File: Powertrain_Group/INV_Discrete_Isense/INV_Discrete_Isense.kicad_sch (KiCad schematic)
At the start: 20 parts, among them J1 Conn_01x04_Socket, J2 Conn_01x04_Socket, J3 Conn_01x04_Socket, J4 15130122601000, J5 DF1E-2P-2.5DS_35_, J6 DF1E-2P-2.5DS_35_, U7 AMC3330

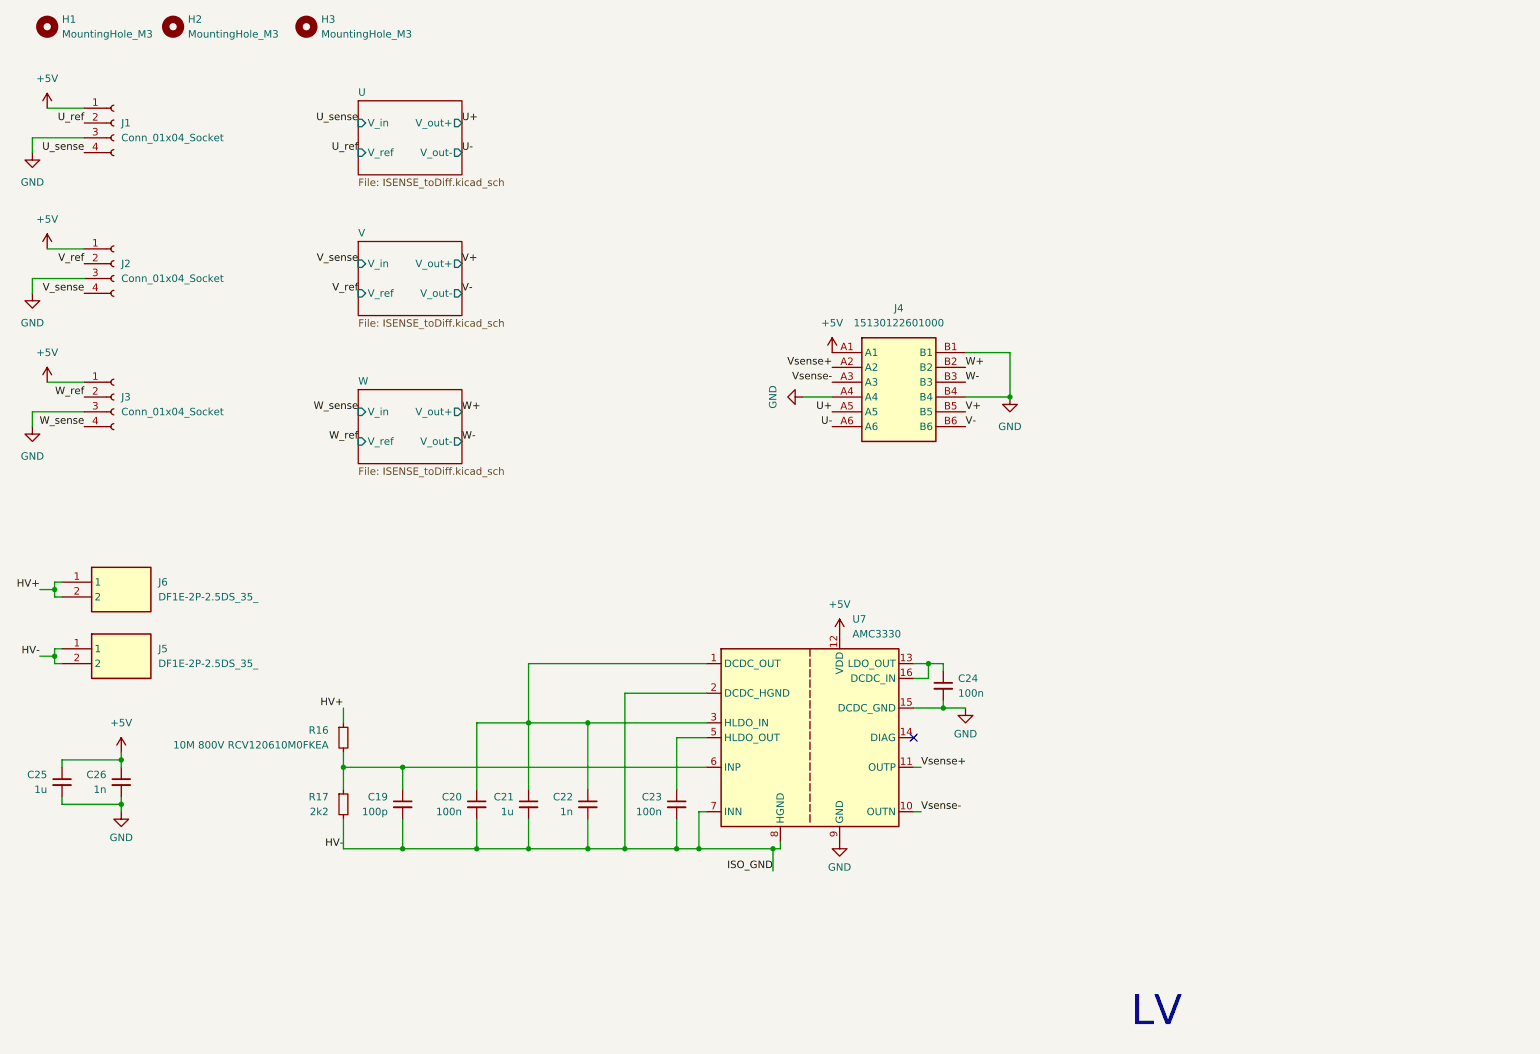
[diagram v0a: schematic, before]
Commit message: [INV_Discrete_Isense] V1.1
and update library for it
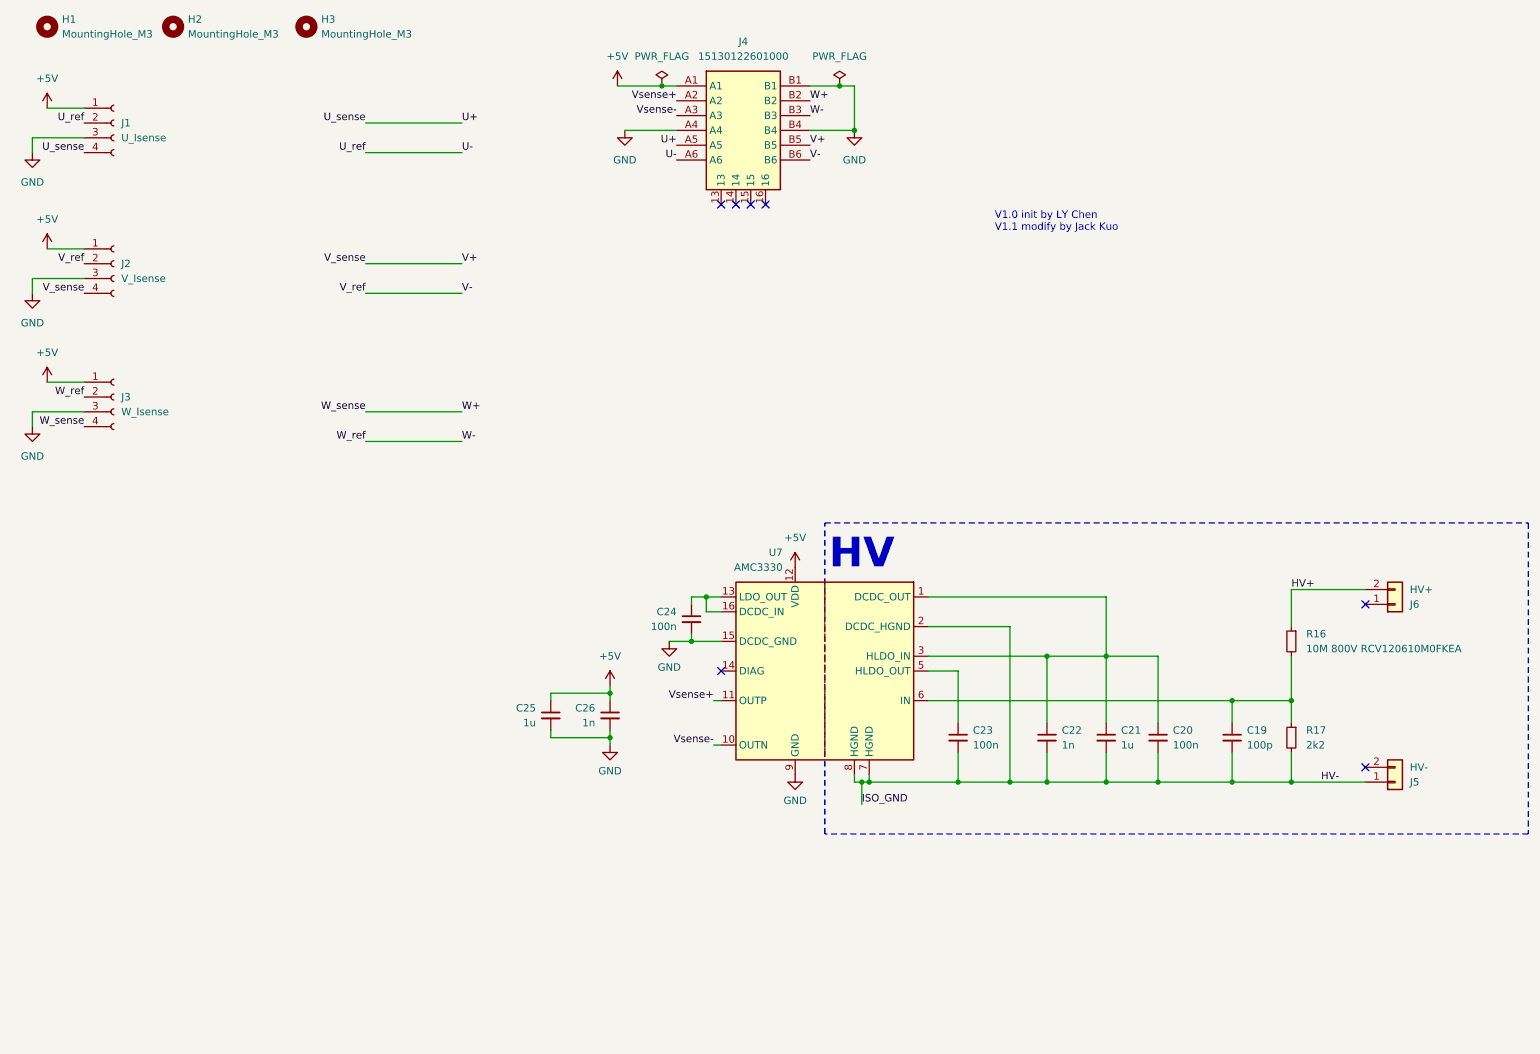
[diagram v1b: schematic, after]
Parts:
- J1: value Conn_01x04_Socket -> U_Isense
- J2: value Conn_01x04_Socket -> V_Isense
- J3: value Conn_01x04_Socket -> W_Isense
- J4: footprint 15130122601000 -> nturt_kicad_lib_EP7:Harting_15130122601000; symbol 15130122601000:15130122601000 -> nturt_kicad_lib_EP7:Harting_15130122601000
- J5: value DF1E-2P-2.5DS_35_ -> HV-; footprint DF1E2P25DS35 -> nturt_kicad_lib_EP7:Hirose_DF1E2P25DS35; symbol DF1E-2P-2_5DS_35_:DF1E-2P-2.5DS_35_ -> Connector_Generic:Conn_01x02
- J6: value DF1E-2P-2.5DS_35_ -> HV+; footprint DF1E2P25DS35 -> nturt_kicad_lib_EP7:Hirose_DF1E2P25DS35; symbol DF1E-2P-2_5DS_35_:DF1E-2P-2.5DS_35_ -> Connector_Generic:Conn_01x02
- U7: symbol Isolator_Analog:AMC3330 -> nturt_kicad_lib_EP7:AMC3311
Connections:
- net U_ref is gone; now on net U-: J1.2 (Pin_2)
- net U_sense is gone; now on net U+: J1.4 (Pin_4)
- net V_ref is gone; now on net V-: J2.2 (Pin_2)
- net V_sense is gone; now on net V+: J2.4 (Pin_4)
- net W_ref is gone; now on net W-: J3.2 (Pin_2)
- net W_sense is gone; now on net W+: J3.4 (Pin_4)
- net HV+: no longer J6.1
- net HV-: no longer J5.2
- no-connect marks 1 -> 7
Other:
- removed sheet U
- removed sheet V
- removed sheet W
- note added: "HV"
- note added: "V1.0 init by LY Chen V1.1 modify by Jack Kuo"
- note removed: "LV"
- company: (none) -> NTURacing
- title: (none) -> INV_Discrete_Isense
- moved on the sheet: C19, C20, C21, C22, C23, C24, C25, C26, J5, J6, R16, R17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

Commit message: [INV_Discrete_Isense] V1.2
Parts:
- C19, C20, C21, C22, C23, C24, C25, C26: footprint Capacitor_SMD:C_0402_1005Metric -> Capacitor_SMD:C_0603_1608Metric
- U7: value AMC3330 -> AMC3311
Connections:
- net U+: now also J4.A6; no longer J1.4 (Pin_4), J4.A5
- net U-: now also J4.A5; no longer J1.2 (Pin_2), J4.A6
- net V+: now also J4.B6; no longer J2.4 (Pin_4), J4.B5
- net V-: now also J4.B5; no longer J2.2 (Pin_2), J4.B6
- net W+: now also J4.B3; no longer J3.4 (Pin_4), J4.B2
- net W-: now also J4.B2; no longer J3.2 (Pin_2), J4.B3
- new net U_ref: J1.2 (Pin_2)
- new net U_sense: J1.4 (Pin_4)
- new net V_ref: J2.2 (Pin_2)
- new net V_sense: J2.4 (Pin_4)
- new net W_ref: J3.2 (Pin_2)
- new net W_sense: J3.4 (Pin_4)
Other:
- added sheet U (ISENSE_toDiff.kicad_sch)
- added sheet V (ISENSE_toDiff.kicad_sch)
- added sheet W (ISENSE_toDiff.kicad_sch)
- note added: "V1.0 init by Kyle Ho V1.1 modify by Jack Kuo V1.2 modify by Keyle Ho"
- note removed: "V1.0 init by LY Chen V1.1 modify by Jack Kuo"
- moved on the sheet: C19, C20, C21, C22, C23, J6, R16, R17

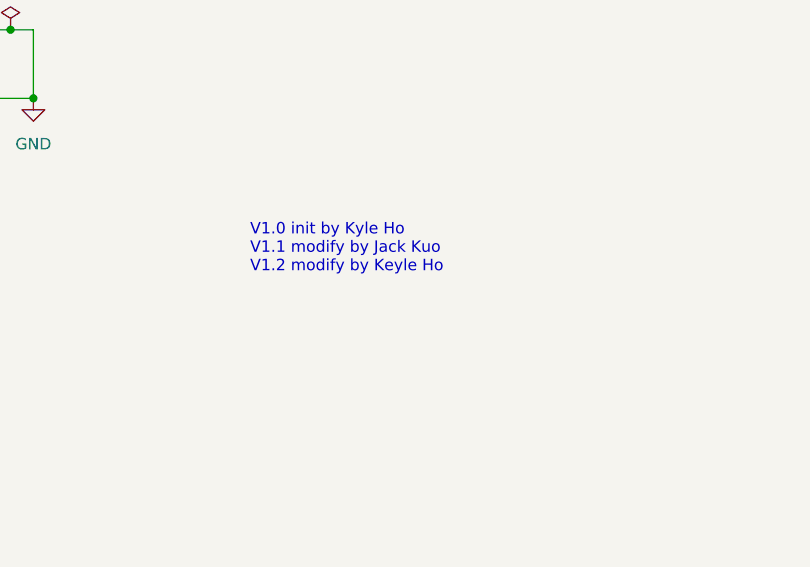
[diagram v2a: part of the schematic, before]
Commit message: [INV_Discete_Isense] V1.2 again
change gain 1 to 2
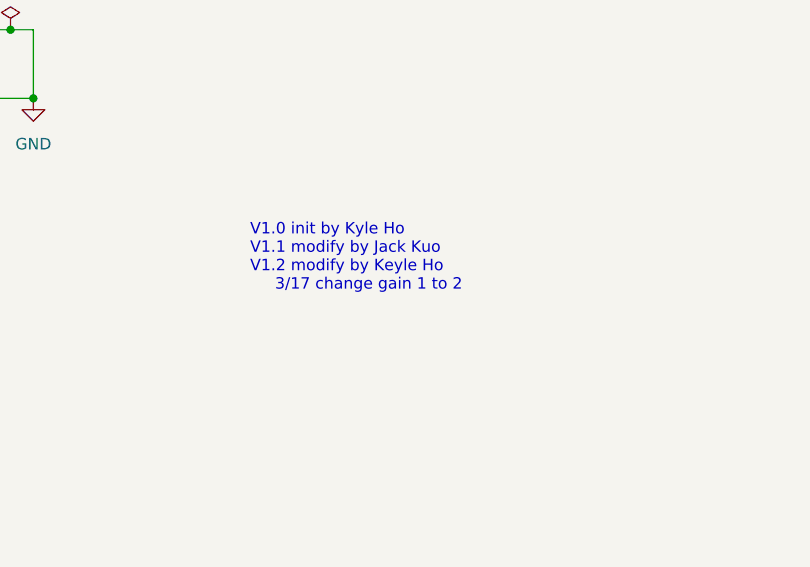
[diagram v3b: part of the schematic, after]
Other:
- note added: "V1.0 init by Kyle Ho V1.1 modify by Jack Kuo V1.2 modify by Keyle Ho 3/17 change gain 1 to 2"
- note removed: "V1.0 init by Kyle Ho V1.1 modify by Jack Kuo V1.2 modify by Keyle Ho"
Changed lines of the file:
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@@
 		)
 	)
-	(text "V1.0 init by Kyle Ho\nV1.1 modify by Jack Kuo\nV1.2 modify by Keyle Ho"
+	(text "V1.0 init by Kyle Ho\nV1.1 modify by Jack Kuo\nV1.2 modify by Keyle Ho\n     3/17 change gain 1 to 2"
 		(exclude_from_sim no)
 		(at 187.9123 54.5657 0)

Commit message: [INV_Discrete_Isense] V1.3
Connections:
- net U_ref is gone; now on net U-: J1.2 (Pin_2)
- net U_sense is gone; now on net U+: J1.4 (Pin_4)
- net V_ref is gone; now on net V-: J2.2 (Pin_2)
- net V_sense is gone; now on net V+: J2.4 (Pin_4)
- net W_ref is gone; now on net W-: J3.2 (Pin_2)
- net W_sense is gone; now on net W+: J3.4 (Pin_4)
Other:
- removed sheet U
- removed sheet V
- removed sheet W
- note added: "V1.0 init by Kyle Ho V1.1 modify by Jack Kuo V1.2 modify by Keyle Ho 3/17 change gain 1 to 2 V1.3 remove amplifier"
- note removed: "V1.0 init by Kyle Ho V1.1 modify by Jack Kuo V1.2 modify by Keyle Ho 3/17 change gain 1 to 2"
